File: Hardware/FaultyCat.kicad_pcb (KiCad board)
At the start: 2 copper layers, 51.2 x 124.2 mm, 137 parts, among them J1 Antenna, J10 TRIGGER_VREF, J2 BG306-02-A-2-0400-L-G, J3 Conn_01x10, J4 Header 2, J5 Header 4, J6 Input Power:2x AA Battery, J7 GLITCHER_EN, J8 ANALOG_PINS, J9 TRIGGER_IN, P1 USB_C_Plug_USB2.0, Q1 AO3422, Q2 AO3422, Q3 LDA111STR, Q4 RGT16BM65DTL, Q5 DMG3415U-7, Q7 IRLML2502, Q8 IRF7807PBF, SW1 TL3305AF260QG, SW2 ON, SW3 TL3305AF260QG, SW4 RESET, SW5 BOOT, SW6 TL3305AF260QG, SW7 SW_SP3T, T1 ATB322524, T2 ATB322524, U1 AP2112K-3.3, U2 W25Q16JV, U3 RP2040, U4 TXS0108EPW, U5 TLV75718PDBV, U6 SN74LVC1T45DBV, Y1 12Mhz

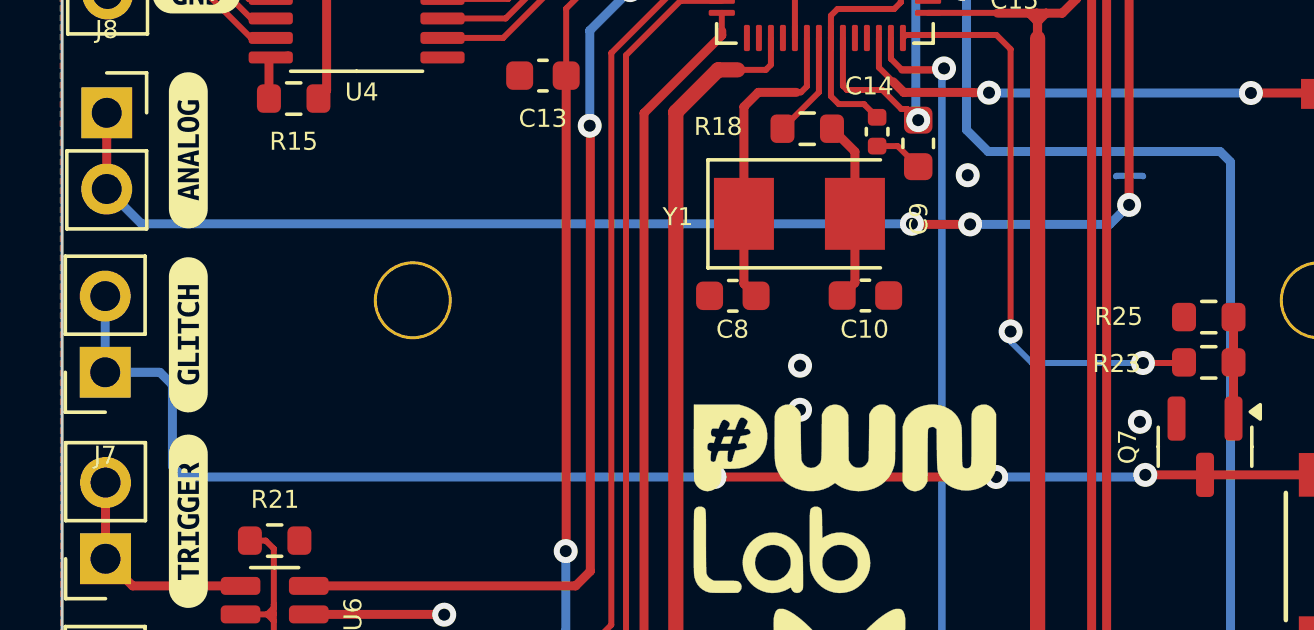
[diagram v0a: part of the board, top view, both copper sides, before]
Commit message: feat(Hw):Update_Traces
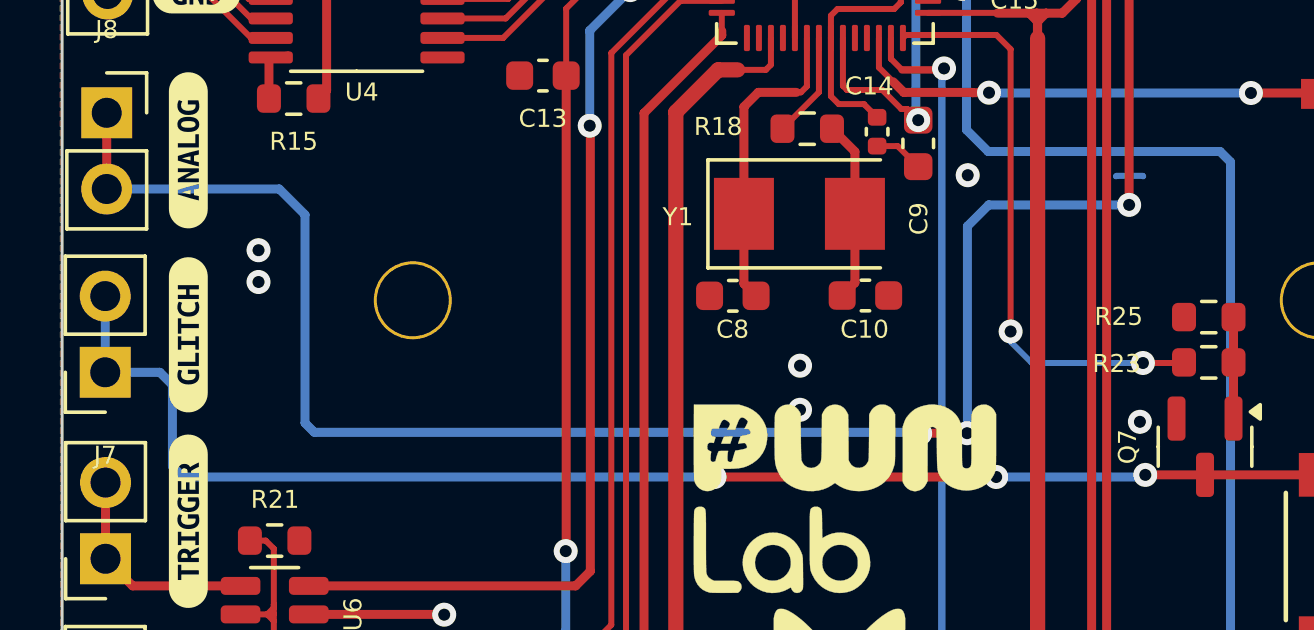
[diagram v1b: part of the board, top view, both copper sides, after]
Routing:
- net /ANALOG: track 55.2 -> 69.1 mm
- net GND: vias 26 -> 28
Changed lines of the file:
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@@
 				(font
 					(size 0.001 0.001)
+					(thickness 0.15)
 				)
 			)
@@
 				(font
 					(size 0.001 0.001)
+					(thickness 0.15)
 				)
 			)
@@
 				(font
 					(size 0.001 0.001)
+					(thickness 0.15)
 				)
 			)
@@
 				(font
 					(size 0.001 0.001)
+					(thickness 0.15)
 				)
 			)
@@
 				(font
 					(size 0.001 0.001)
+					(thickness 0.15)
 				)
 			)
@@
 				(font
 					(size 0.001 0.001)
+					(thickness 0.15)
 				)
 			)
@@
 				(font
 					(size 0.001 0.001)
+					(thickness 0.15)
 				)
 			)
@@
 				(font
 					(size 0.001 0.001)
+					(thickness 0.15)
 				)
 			)
@@
 	)
 	(via
+		(at 91.6 62.22)
+		(size 0.8)
+		(drill 0.4)
+		(layers "F.Cu" "B.Cu")
+		(free yes)
+		(net 2)
+	)
+	(via
 		(at 118.78 38.93)
 		(size 0.8)
@@
 	)
 	(via
+		(at 91.6 61.16)
+		(size 0.8)
+		(drill 0.4)
+		(layers "F.Cu" "B.Cu")
+		(free yes)
+		(net 2)
+	)
+	(via
 		(at 100 86)
 		(size 0.8)
@@
 	)
 	(segment
-		(start 120.62 59.65)
-		(end 120.62 48.65)
+		(start 113.665 67.26)
+		(end 113.655 67.27)
 		(width 0.3)
 		(layer "F.Cu")
@@
 	)
 	(segment
-		(start 115.32 60.3)
-		(end 113.4 60.3)
+		(start 120.62 59.65)
+		(end 120.62 48.65)
 		(width 0.3)
 		(layer "F.Cu")
@@
 	)
 	(segment
-		(start 113.4 60.3)
-		(end 113.38 60.28)
+		(start 119.63 48.45)
+		(end 119.62875 48.44875)
 		(width 0.3)
 		(layer "F.Cu")
@@
 	)
 	(segment
-		(start 119.63 48.45)
-		(end 119.62875 48.44875)
+		(start 115.22 67.26)
+		(end 113.665 67.26)
 		(width 0.3)
 		(layer "F.Cu")
@@
 	)
 	(via
-		(at 115.32 60.3)
+		(at 115.22 67.26)
 		(size 0.8)
 		(drill 0.4)
@@
 	)
 	(via
-		(at 113.38 60.28)
+		(at 113.655 67.27)
 		(size 0.8)
 		(drill 0.4)
@@
 	)
 	(segment
-		(start 119.97 60.3)
-		(end 115.32 60.3)
+		(start 113.655 67.27)
+		(end 113.37 67.27)
 		(width 0.3)
 		(layer "B.Cu")
@@
 	)
 	(segment
-		(start 87.7 60.28)
-		(end 86.54 59.12)
+		(start 115.22 67.26)
+		(end 115.23 67.25)
 		(width 0.3)
 		(layer "B.Cu")
@@
 	)
 	(segment
-		(start 113.38 60.28)
-		(end 87.7 60.28)
+		(start 113.37 67.27)
+		(end 113.33 67.23)
 		(width 0.3)
 		(layer "B.Cu")
@@
 	)
 	(segment
-		(start 120.62 59.65)
-		(end 119.97 60.3)
+		(start 93.46 67.23)
+		(end 93.15 66.92)
+		(width 0.3)
+		(layer "B.Cu")
+		(net 73)
+	)
+	(segment
+		(start 113.33 67.23)
+		(end 93.46 67.23)
+		(width 0.3)
+		(layer "B.Cu")
+		(net 73)
+	)
+	(segment
+		(start 93.15 59.98)
+		(end 92.29 59.12)
+		(width 0.3)
+		(layer "B.Cu")
+		(net 73)
+	)
+	(segment
+		(start 115.94 59.65)
+		(end 120.62 59.65)
+		(width 0.3)
+		(layer "B.Cu")
+		(net 73)
+	)
+	(segment
+		(start 115.23 60.36)
+		(end 115.94 59.65)
+		(width 0.3)
+		(layer "B.Cu")
+		(net 73)
+	)
+	(segment
+		(start 93.15 66.92)
+		(end 93.15 59.98)
+		(width 0.3)
+		(layer "B.Cu")
+		(net 73)
+	)
+	(segment
+		(start 115.23 67.25)
+		(end 115.23 60.36)
+		(width 0.3)
+		(layer "B.Cu")
+		(net 73)
+	)
+	(segment
+		(start 92.29 59.12)
+		(end 86.54 59.12)
 		(width 0.3)
 		(layer "B.Cu")

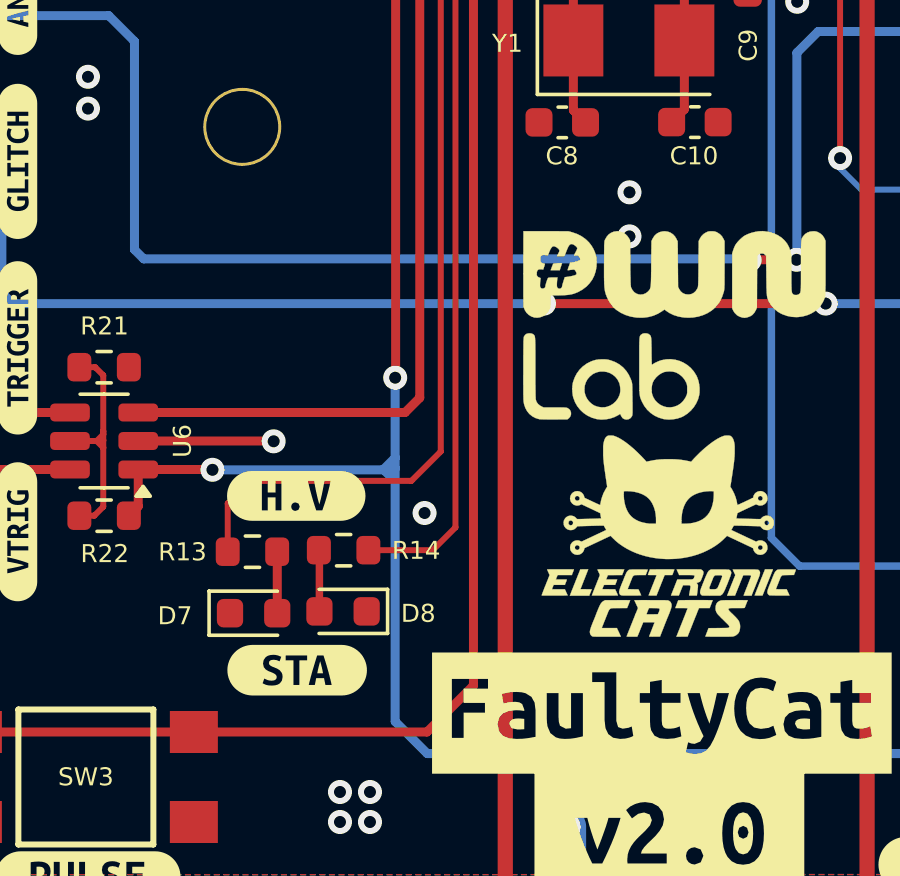
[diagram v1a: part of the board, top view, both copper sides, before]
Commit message: fix(hw): move labels
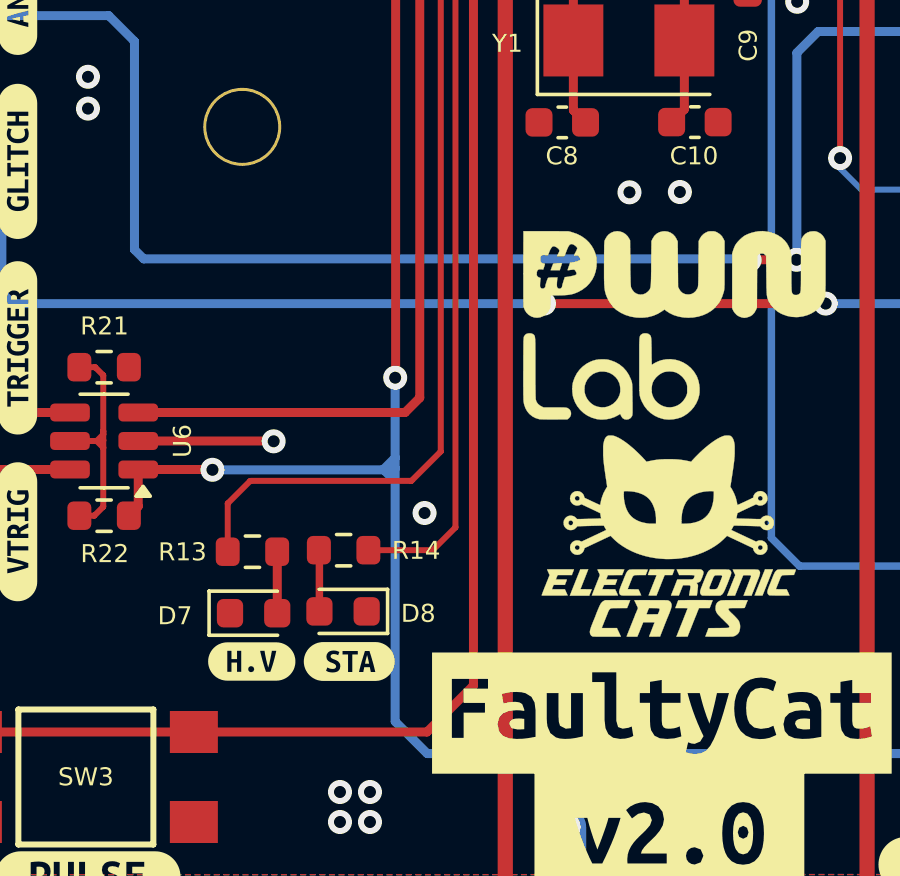
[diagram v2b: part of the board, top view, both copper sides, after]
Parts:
- removed kibuzzard-642DF6A9: G***, kibuzzard-642DF6A9
- removed kibuzzard-642DF6E0: G***, kibuzzard-642DF6E0
- added kibuzzard-67AA52CA: G***, kibuzzard-67AA52CA, F.Cu at (97.1, 80.7)
- added kibuzzard-67AA52D2: G***, kibuzzard-67AA52D2, F.Cu at (100.3, 80.7)

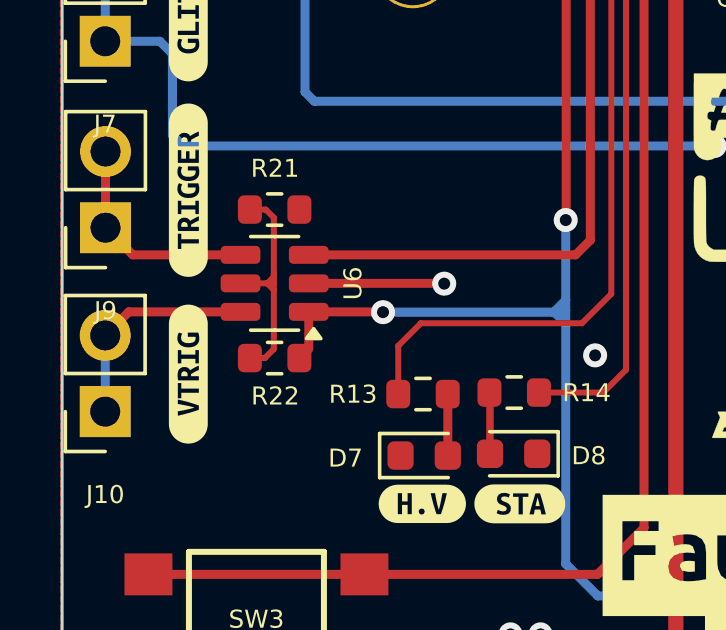
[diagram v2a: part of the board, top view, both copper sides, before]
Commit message: feat: delete dnp resistor
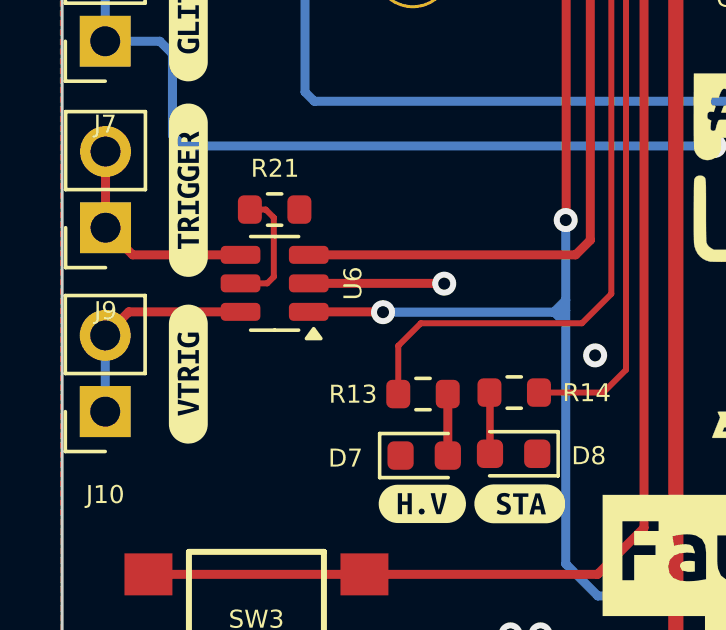
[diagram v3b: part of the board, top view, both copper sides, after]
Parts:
- removed R22: R, Resistor_SMD:R_0603_1608Metric
- C11, C12, C14, C15, C16, C17, C18, C19, C20, C21, C22, C7: value 0.1uF -> 100nF
- R21: value R -> 10k
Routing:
- net Net-(U6-DIR): track 8.06 -> 4.08 mm
- net +3V3: track 236.6 -> 234.9 mm

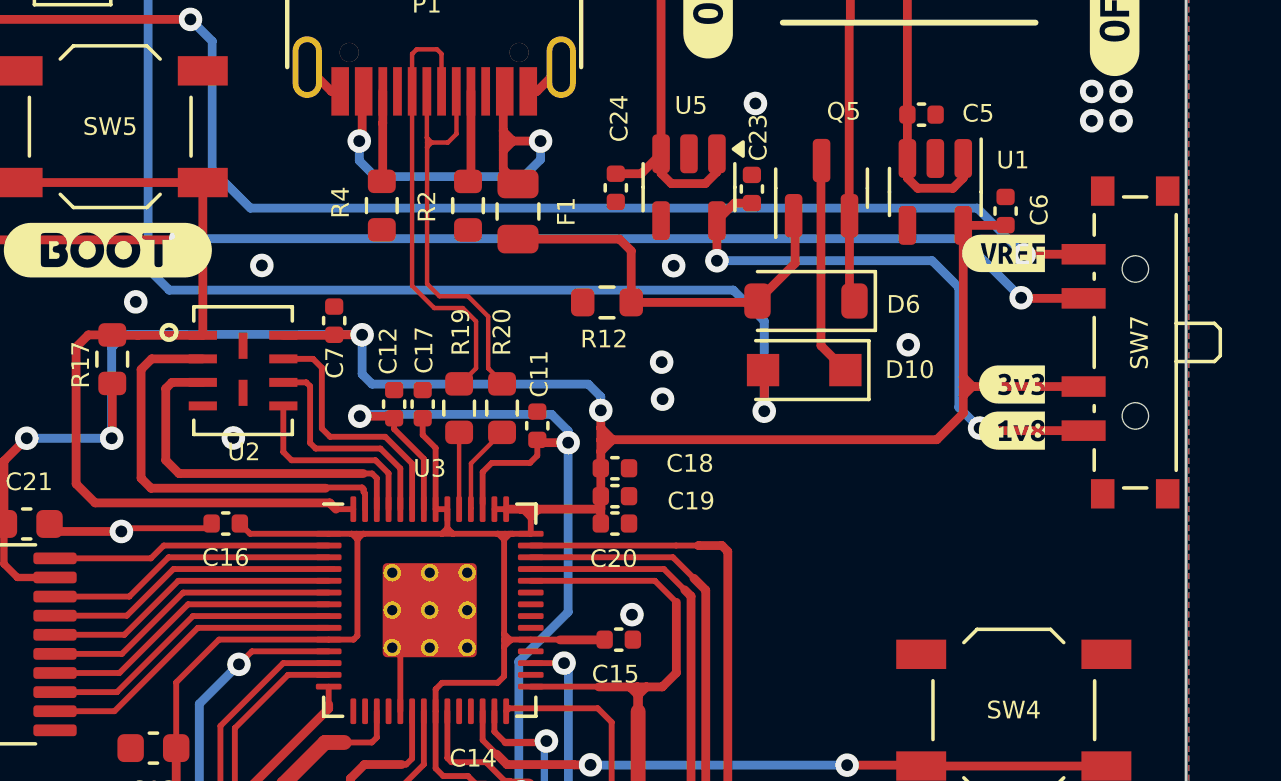
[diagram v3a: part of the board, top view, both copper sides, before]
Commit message: feat(hw): change selector switch
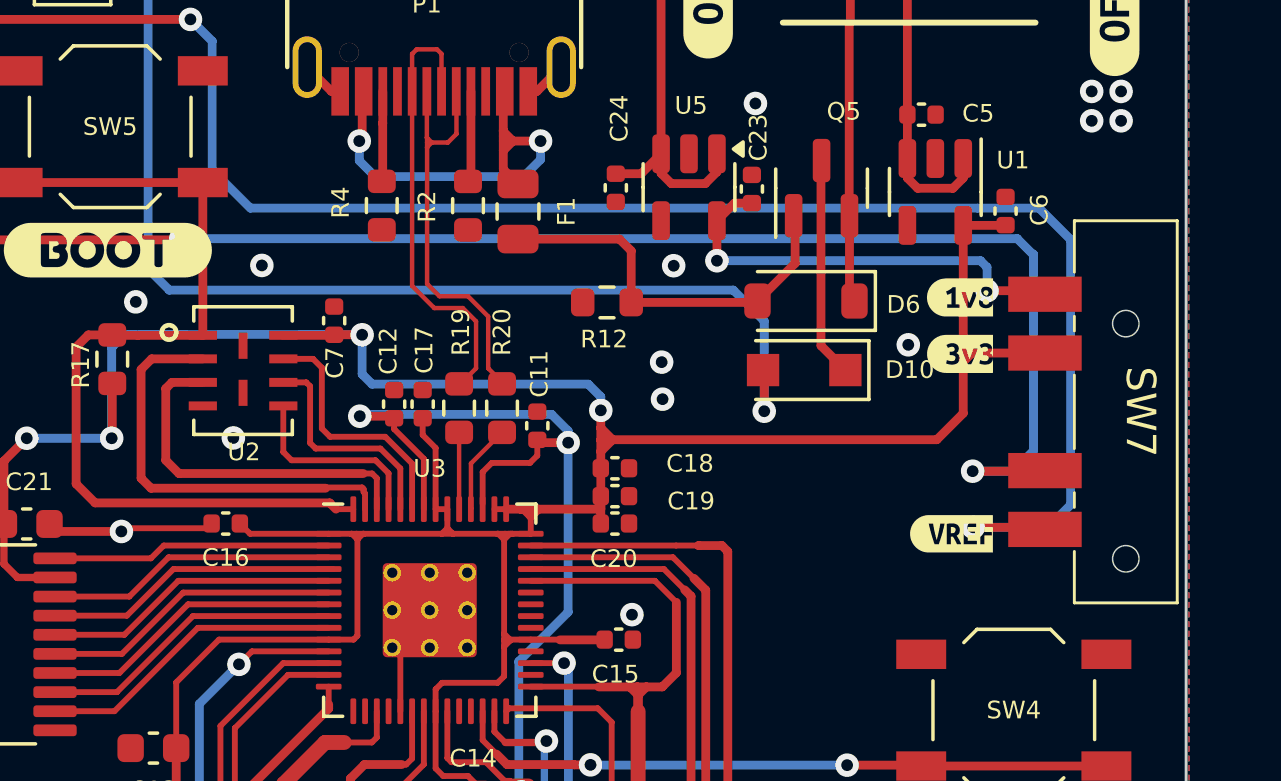
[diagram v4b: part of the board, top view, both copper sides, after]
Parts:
- SW7: footprint Button_Switch_SMD:SW_SP3T_PCM13 -> BuggyCat:Sw3P1T
- moved kibuzzard-67AA35C3 9.70 mm to (128.2, 48.0)
- moved kibuzzard-67AA359F 4.86 mm to (128.5, 40.0)
- moved SW7 2.36 mm to (134.2, 43.9), turned to -90 degrees
- moved kibuzzard-67AA35B7 2.05 mm to (128.5, 41.9)
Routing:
- net /VREF: track 52.4 -> 66.8 mm
- net /VREFOUT: track 59.9 -> 69.0 mm
- net +1V8: track 20.1 -> 14.9 mm
- net +3V3: track 234.9 -> 233.5 mm

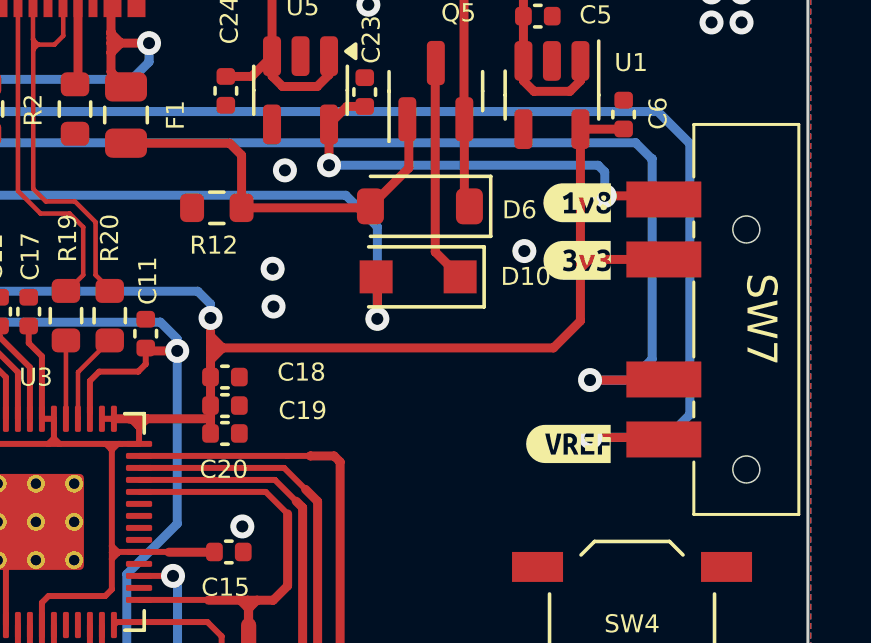
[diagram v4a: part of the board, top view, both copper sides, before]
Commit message: fix(hw): move labels
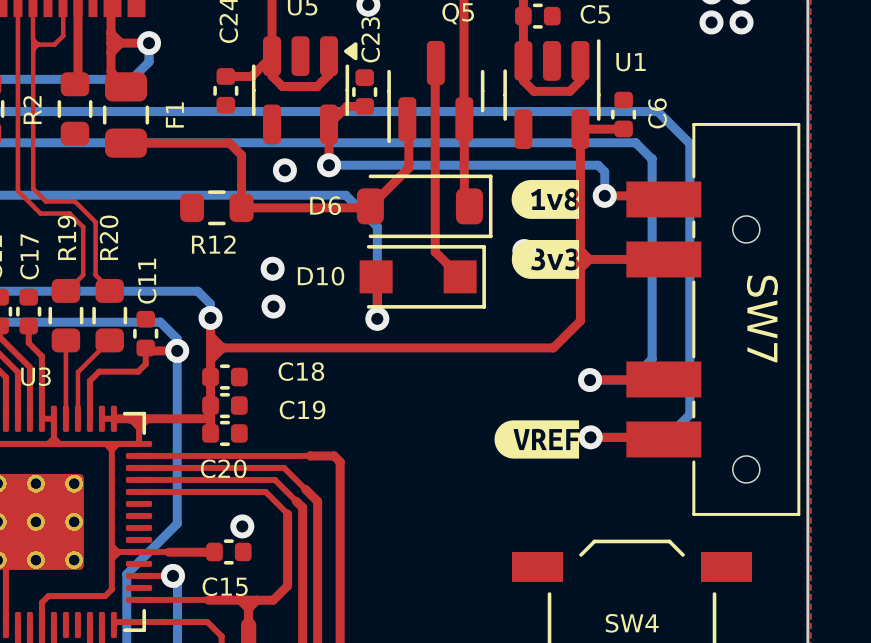
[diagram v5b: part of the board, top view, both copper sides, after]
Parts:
- moved kibuzzard-67AA359F 1.07 mm to (127.5, 39.9)
- moved kibuzzard-67AA35C3 1.07 mm to (127.2, 47.9)
- moved kibuzzard-67AA35B7 1.06 mm to (127.5, 41.9)
